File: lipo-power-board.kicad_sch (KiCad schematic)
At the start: 18 parts, among them U1 TPS61092, U2 MCP73871-1CA

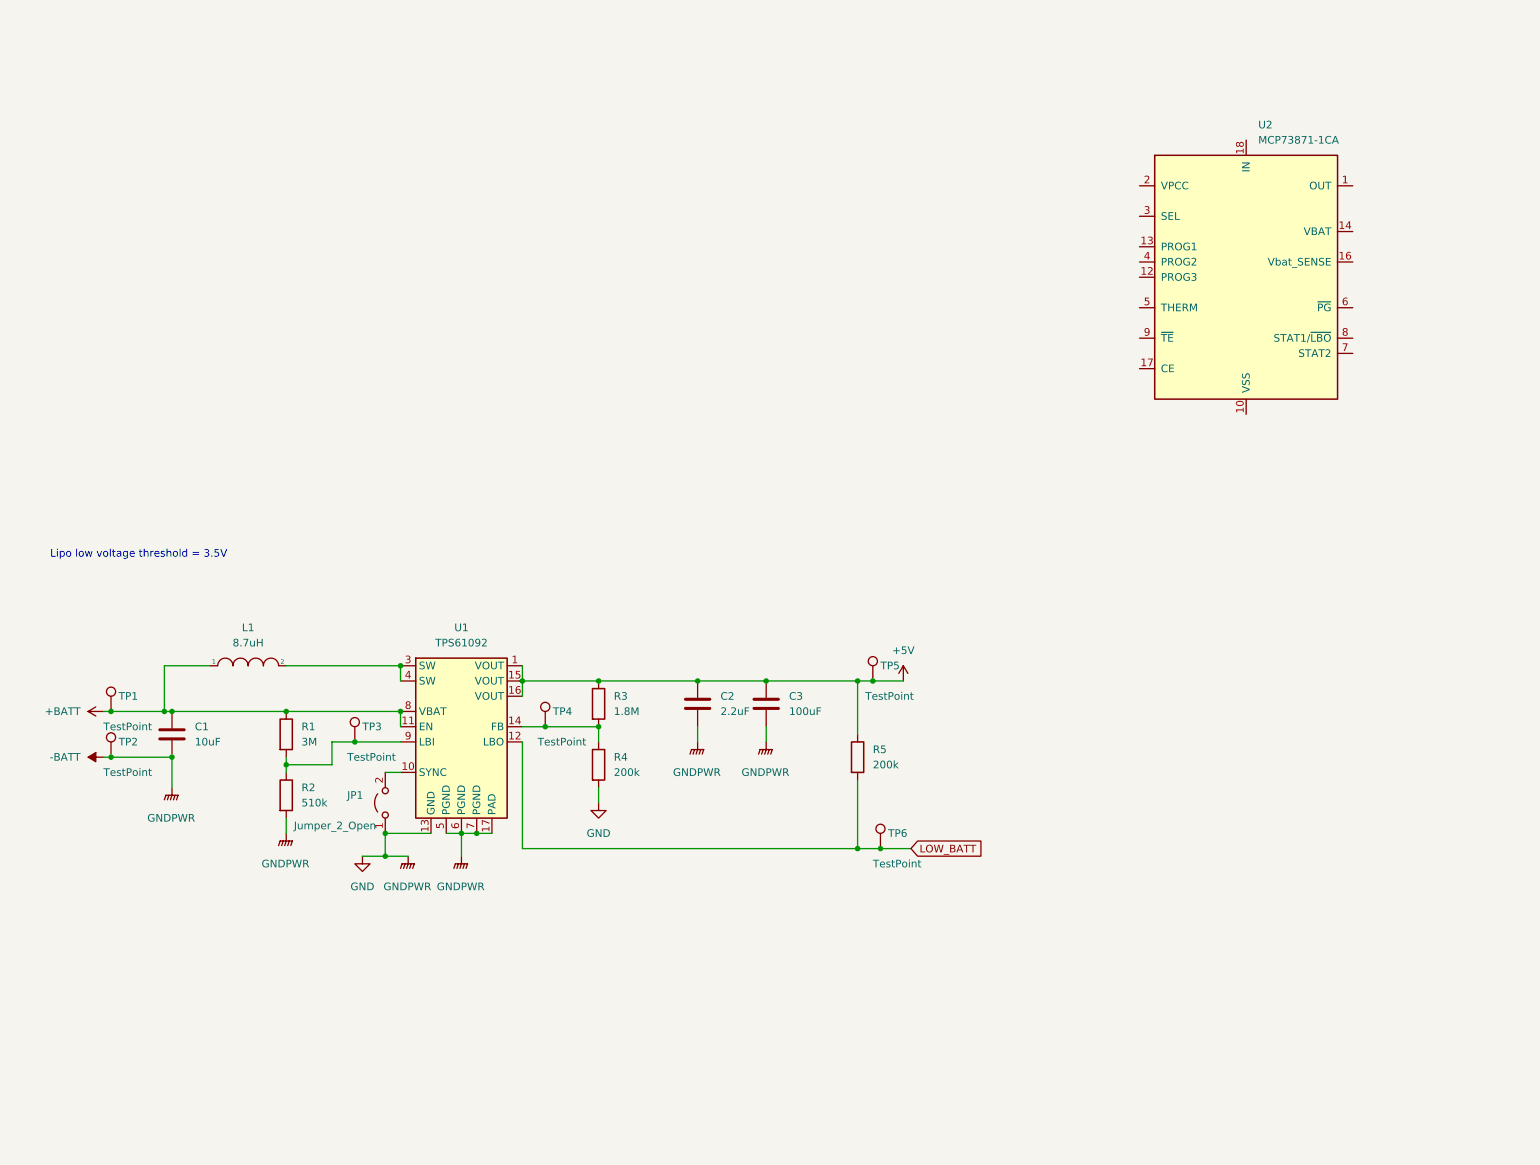
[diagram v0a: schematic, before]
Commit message: Lay out charger circuit
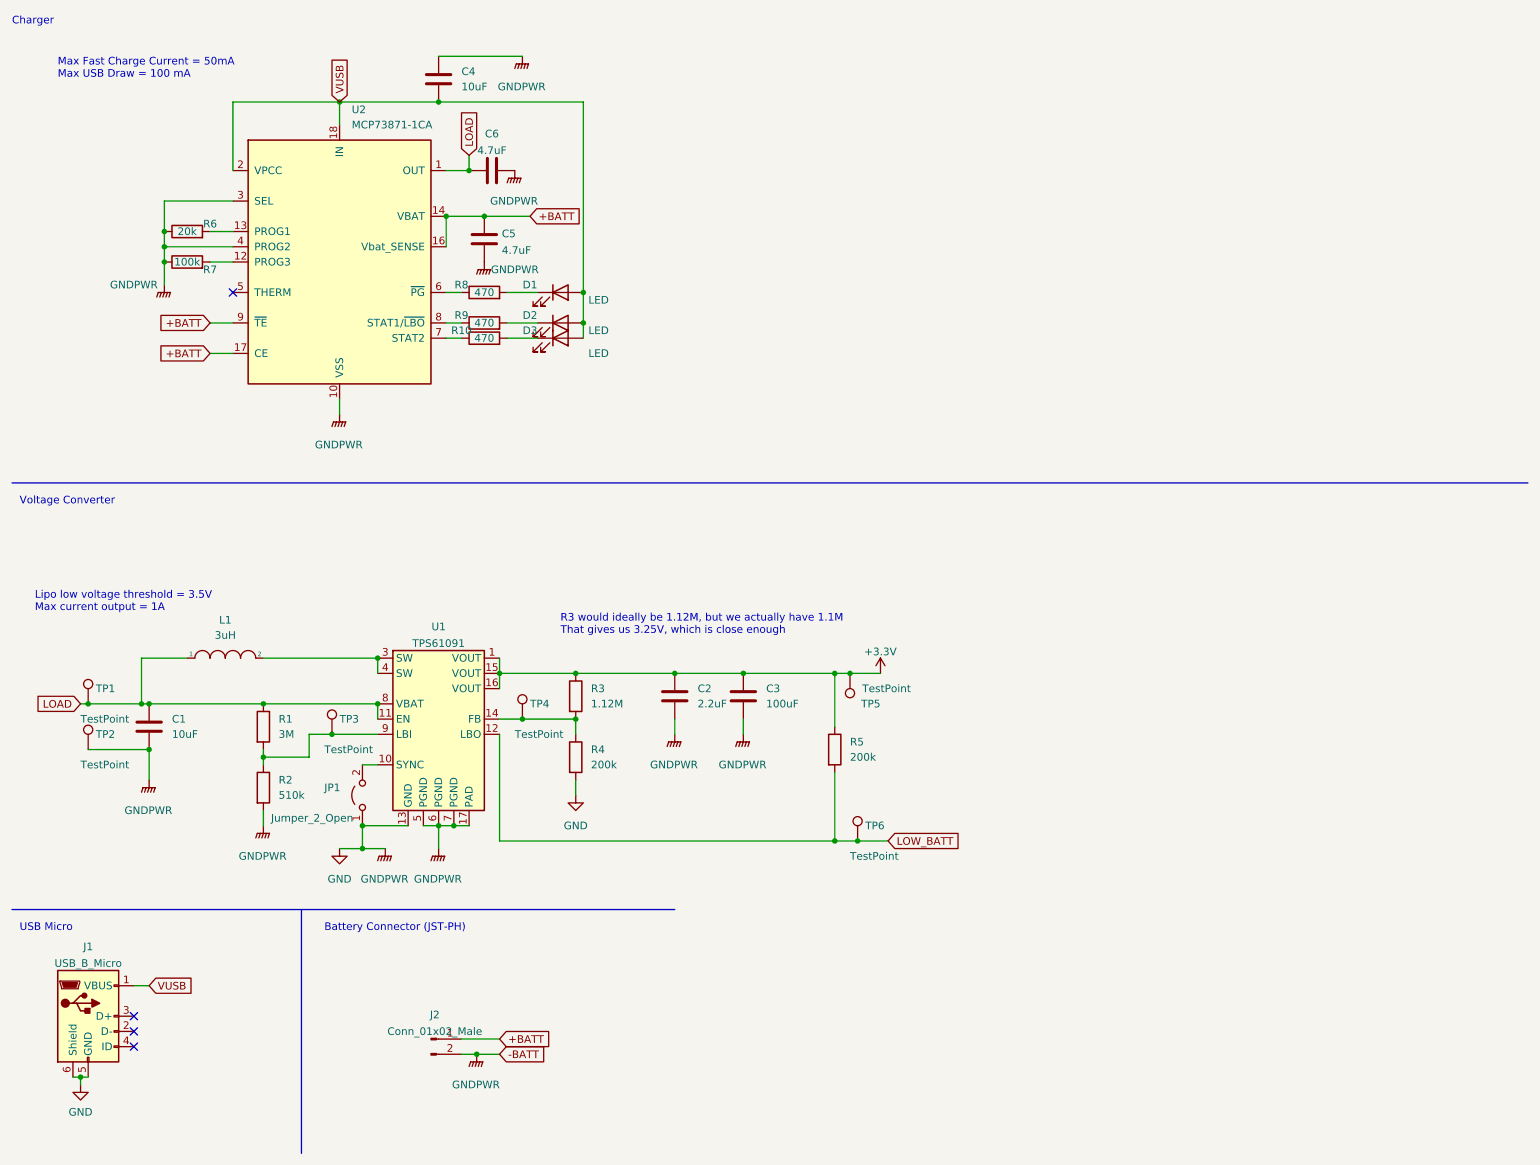
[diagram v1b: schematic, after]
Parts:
- removed U1: TPS61092, Package_DFN_QFN:Texas_S-PVQFN-N16_EP2.7x2.7mm_ThermalVias, symbol Regulator_Switching:TPS61092
- added C4: 10uF, Capacitor_SMD:C_0805_2012Metric, symbol Device:C
- added C5, C6: 4.7uF, Capacitor_SMD:C_0805_2012Metric, symbol Device:C
- added D1, D2, D3: LED, LED_SMD:LED_0805_2012Metric, symbol Device:LED
- added J1: USB_B_Micro, Connector_USB:USB_Micro-B_Amphenol_10118194_Horizontal, symbol Connector:USB_B_Micro
- added J2: Conn_01x02_Male, Connector_JST:JST_PH_S2B-PH-K_1x02_P2.00mm_Horizontal, symbol Connector:Conn_01x02_Male
- added R10, R8, R9: 470, Resistor_SMD:R_0805_2012Metric, symbol Device:R
- added R6: 20k, Resistor_SMD:R_0805_2012Metric, symbol Device:R
- added R7: 100k, Resistor_SMD:R_0805_2012Metric, symbol Device:R
- added U1: TPS61091, Package_DFN_QFN:Texas_S-PVQFN-N16_EP2.7x2.7mm_ThermalVias, symbol Regulator_Switching:TPS61091
- L1: value 8.7uH -> 3uH; Digikey # 2457-MSS7341-872NLD-ND -> 308-1495-2-ND
- R3: value 1.8M -> 1.12M; Digikey # P1.80MCTR-ND -> 311-1.10MCRTR-ND
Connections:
- net -BATT is gone; now on net GND: C1.2, C2.2, C3.2, JP1.1 (A), R2.2, R4.2, TP2.1
- net +BATT: now also U2.14 (VBAT), U2.15 (VBAT), U2.16 (Vbat_SENSE), U2.17 (CE), U2.9 (~{TE}), C5.1, J2.1 (Pin_1); no longer C1.1, L1.1, R1.1, TP1.1
- net LOW_BATT: now also U1.12 (LBO)
- net at JP1.2 (B): now also U1.10 (SYNC)
- net at R3.2, R4.1, TP4.1: now also U1.14 (FB)
- net at L1.2: now also U1.3 (SW), U1.4 (SW)
- net at R1.2, R2.1, TP3.1: now also U1.9 (LBI)
- net LOAD: now reaches U2.1 (OUT), U2.20 (OUT)
- net LOAD: now also C1.1, L1.1, R1.1, TP1.1, C6.1, U1.11 (EN), U1.8 (VBAT)
- net GND: now reaches U2.10 (VSS), U2.11 (VSS), U2.21 (VSS)
- net GND: now also U2.3 (SEL), U2.4 (PROG2), C4.1, C5.2, C6.2, J1.5 (GND), J1.6 (Shield), J2.2 (Pin_2), R6.1, R7.1, U1.13 (GND), U1.17 (PAD), U1.5 (PGND), U1.6 (PGND), U1.7 (PGND)
- net at U2.12 (PROG3): now also R7.2
- net at U2.13 (PROG1): now also R6.2
- net VUSB: now reaches U2.18 (IN), U2.19 (IN)
- net VUSB: now also U2.2 (VPCC), C4.2, D1.2 (A), D2.2 (A), D3.2 (A), J1.1 (VBUS)
- net at U2.6 (~{PG}): now also R8.1
- net at U2.7 (STAT2): now also R10.1
- net at U2.8 (STAT1/~{LBO}): now also R9.1
- net +5V renamed +3V3
- net +3V3: now also U1.1 (VOUT), U1.15 (VOUT), U1.16 (VOUT)
- new net: D1.1 (K), R8.2
- new net: D3.1 (K), R10.2
- new net: D2.1 (K), R9.2
- no-connect marks 0 -> 4
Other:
- note added: "Battery Connector (JST-PH)"
- note added: "Charger"
- note added: "Lipo low voltage threshold = 3.5V Max current output = 1A"
- note added: "Max Fast Charge Current = 50mA Max USB Draw = 100 mA"
- note added: "R3 would ideally be 1.12M, but we actually have 1.1M That gives us 3.25V, which is close enough"
- note added: "USB Micro"
- note added: "Voltage Converter"
- note removed: "Lipo low voltage threshold = 3.5V"
- moved on the sheet: C1, C2, C3, JP1, L1, R1, R2, R3, R4, R5, TP1, TP2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

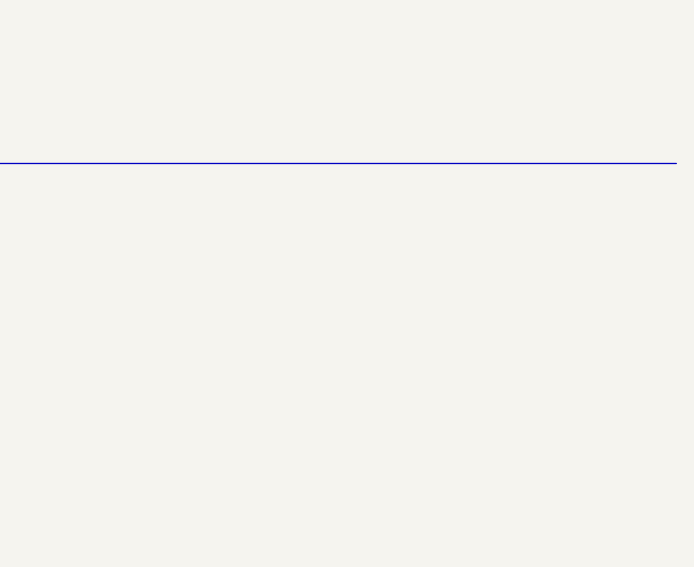
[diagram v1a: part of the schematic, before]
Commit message: External connector
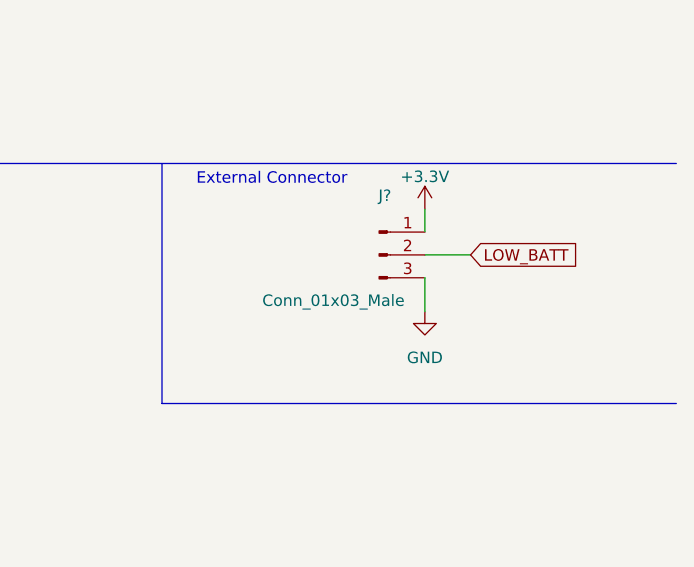
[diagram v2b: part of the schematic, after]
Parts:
- added J?: Conn_01x03_Male, symbol Connector:Conn_01x03_Male
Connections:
- net +3V3: now also J?.1 (Pin_1)
- net GND: now also J?.3 (Pin_3)
- net LOW_BATT: now also J?.2 (Pin_2)
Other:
- note added: "External Connector"
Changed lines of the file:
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@@
+    (stroke (width 0) (type default) (color 0 0 0 0))
+  )
+  (wire (pts (xy 238.76 96.52) (xy 238.76 99.06))
     (stroke (width 0) (type default) (color 0 0 0 0))
   )
@@
     (stroke (width 0) (type default) (color 0 0 0 0))
   )
+  (wire (pts (xy 238.76 104.14) (xy 238.76 107.95))
+    (stroke (width 0) (type default) (color 0 0 0 0))
+  )
   (wire (pts (xy 35.56 128.27) (xy 36.83 128.27))
     (stroke (width 0) (type default) (color 0 0 0 0))
@@
     (stroke (width 0) (type default) (color 0 0 0 0))
   )
+  (polyline (pts (xy 209.55 91.44) (xy 209.55 118.11))
+    (stroke (width 0) (type default) (color 0 0 0 0))
+  )
   (wire (pts (xy 95.25 123.19) (xy 107.95 123.19))
     (stroke (width 0) (type default) (color 0 0 0 0))
   )
+  (polyline (pts (xy 209.55 118.11) (xy 266.7 118.11))
+    (stroke (width 0) (type default) (color 0 0 0 0))
+  )
   (wire (pts (xy 36.83 135.89) (xy 36.83 140.97))
     (stroke (width 0) (type default) (color 0 0 0 0))
@@
   )
   (wire (pts (xy 63.5 133.35) (xy 63.5 137.16))
+    (stroke (width 0) (type default) (color 0 0 0 0))
+  )
+  (wire (pts (xy 238.76 101.6) (xy 243.84 101.6))
     (stroke (width 0) (type default) (color 0 0 0 0))
   )
@@
   (text "Max Fast Charge Current = 50mA\nMax USB Draw = 100 mA"
     (at 21.59 24.13 0)
+    (effects (font (size 1.27 1.27)) (justify left bottom))
+  )
+  (text "External Connector" (at 213.36 93.98 0)
     (effects (font (size 1.27 1.27)) (justify left bottom))
   )
@@
     )
   )
+  (global_label "LOW_BATT" (shape input) (at 243.84 101.6 0) (fields_autoplaced)
+    (effects (font (size 1.27 1.27)) (justify left))
+    (property "Intersheet References" "${INTERSHEET_REFS}" (id 0) (at 255.2356 101.5206 0)
+      (effects (font (size 1.27 1.27)) (justify left) hide)
+    )
+  )
   (global_label "LOAD" (shape input) (at 90.17 36.83 90) (fields_autoplaced)
     (effects (font (size 1.27 1.27)) (justify left))
@@
     (pin "1")
   )
+  (symbol (lib_id "Connector:Conn_01x03_Male") (at 233.68 101.6 0) (unit 1)
+    (in_bom yes) (on_board yes)
+    (property "Reference" "J?" (id 0) (at 234.315 95.0173 0))
+    (property "Value" "Conn_01x03_Male" (id 1) (at 228.6 106.68 0))
+    (property "Footprint" "" (id 2) (at 233.68 101.6 0)
+      (effects (font (size 1.27 1.27)) hide)
+    )
+    (property "Datasheet" "~" (id 3) (at 233.68 101.6 0)
+      (effects (font (size 1.27 1.27)) hide)
+    )
+    (pin "1")
+    (pin "2")
+    (pin "3")
+  )
   (symbol (lib_id "Jumper:Jumper_2_Open") (at 72.39 143.51 90) (unit 1)
     (in_bom yes) (on_board yes)
@@
     )
     (property "Datasheet" "~" (id 3) (at 31.75 135.89 0)
+      (effects (font (size 1.27 1.27)) hide)
+    )
+    (pin "1")
+  )
+  (symbol (lib_id "power:+3.3V") (at 238.76 96.52 0) (unit 1)
+    (in_bom yes) (on_board yes) (fields_autoplaced)
+    (property "Reference" "#PWR?" (id 0) (at 238.76 100.33 0)
+      (effects (font (size 1.27 1.27)) hide)
+    )
+    (property "Value" "+3.3V" (id 1) (at 238.76 92.9155 0))
+    (property "Footprint" "" (id 2) (at 238.76 96.52 0)
+      (effects (font (size 1.27 1.27)) hide)
+    )
+    (property "Datasheet" "" (id 3) (at 238.76 96.52 0)
       (effects (font (size 1.27 1.27)) hide)
     )
@@
     (pin "1")
     (pin "2")
+  )
+  (symbol (lib_id "power:GND") (at 238.76 107.95 0) (unit 1)
+    (in_bom yes) (on_board yes) (fields_autoplaced)
+    (property "Reference" "#PWR?" (id 0) (at 238.76 114.3 0)
+      (effects (font (size 1.27 1.27)) hide)
+    )
+    (property "Value" "GND" (id 1) (at 238.76 113.03 0))
+    (property "Footprint" "" (id 2) (at 238.76 107.95 0)
+      (effects (font (size 1.27 1.27)) hide)
+    )
+    (property "Datasheet" "" (id 3) (at 238.76 107.95 0)
+      (effects (font (size 1.27 1.27)) hide)
+    )
+    (pin "1")
   )
   (symbol (lib_id "Battery_Management:MCP73871-1CA") (at 68.58 54.61 0) (unit 1)
@@
       (reference "#PWR0116") (unit 1) (value "GNDPWR") (footprint "")
     )
+    (path "/751b1a64-b053-4522-a79b-60f9c639634c"
+      (reference "#PWR?") (unit 1) (value "+3.3V") (footprint "")
+    )
+    (path "/929174ab-9e67-4693-b576-3891bef6f414"
+      (reference "#PWR?") (unit 1) (value "GND") (footprint "")
+    )
     (path "/97b5bd17-bb35-4b1a-8650-263c4447a3e6"
       (reference "C1") (unit 1) (value "10uF") (footprint "Capacitor_SMD:C_0805_2012Metric")
@@
       (reference "J2") (unit 1) (value "Conn_01x02_Male") (footprint "Connector_JST:JST_PH_S2B-PH-K_1x02_P2.00mm_Horizontal")
     )
+    (path "/5f23e1cf-a051-4b96-b66e-6f9291d2776e"
+      (reference "J?") (unit 1) (value "Conn_01x03_Male") (footprint "")
+    )
     (path "/60e8a1ad-bc73-48f2-8f8f-02b96ded4368"
